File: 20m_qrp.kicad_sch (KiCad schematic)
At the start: 28 parts

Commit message: Export schematic for online viewing
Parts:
- gave numbers to parts that had none: 28
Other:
- company: (none) -> BARC <https://bellbrookarc.org/>
- title: (none) -> 20m QRP transceiver

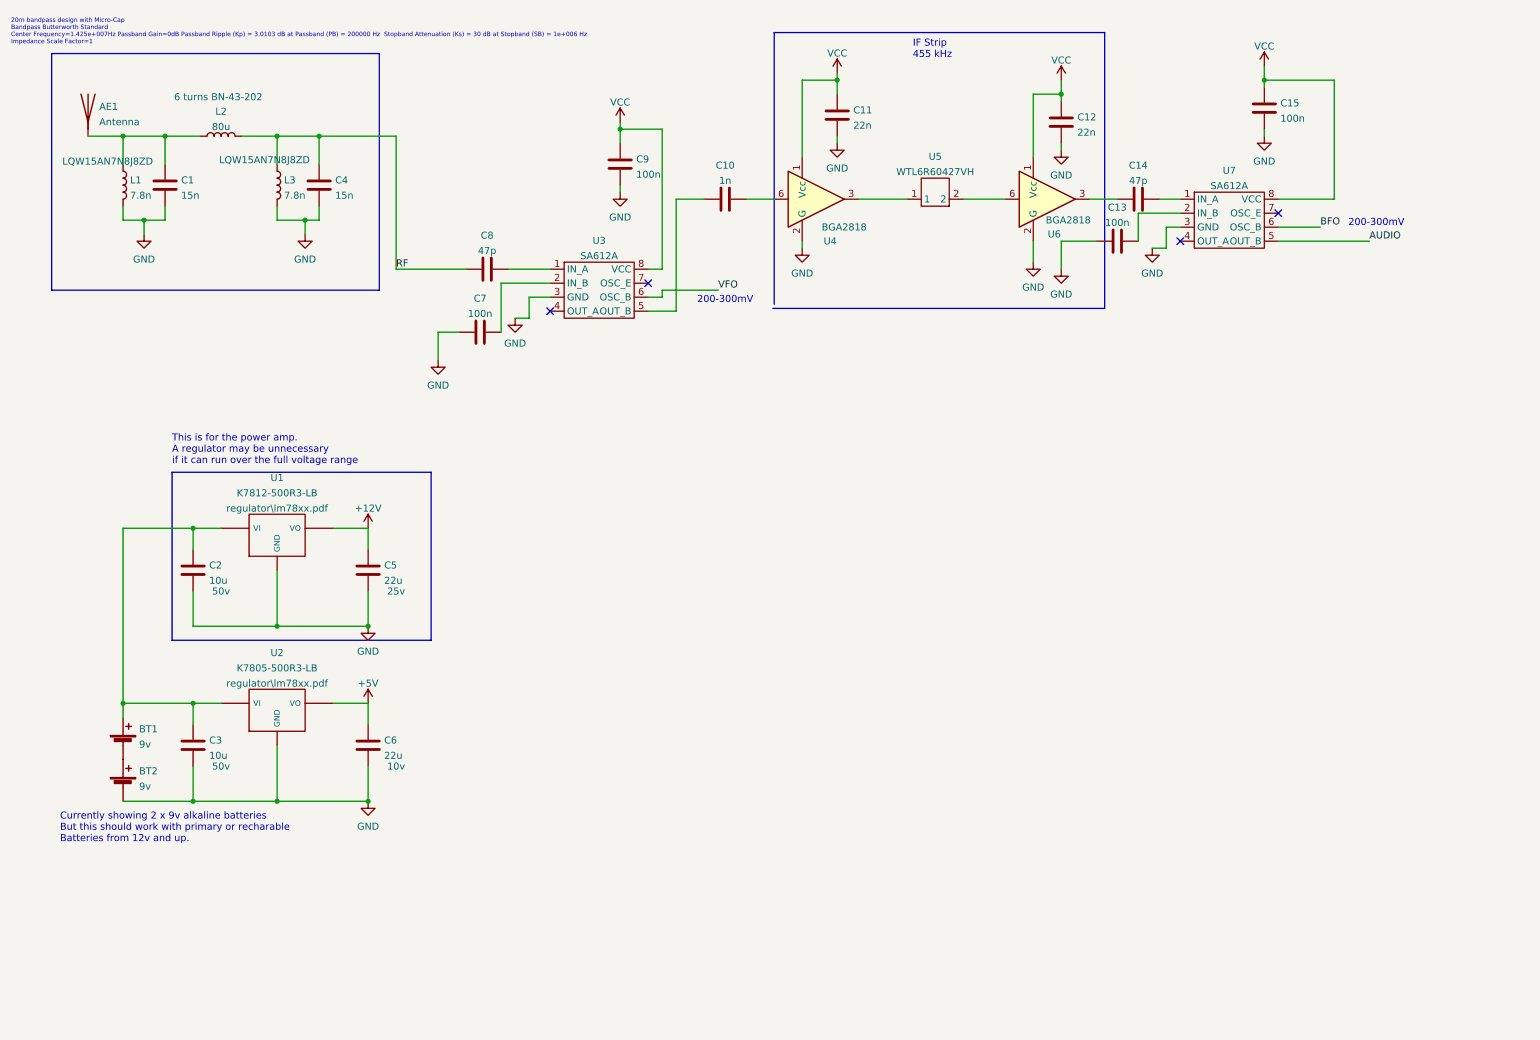
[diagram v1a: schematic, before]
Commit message: Add IF filter match and oscillator sections
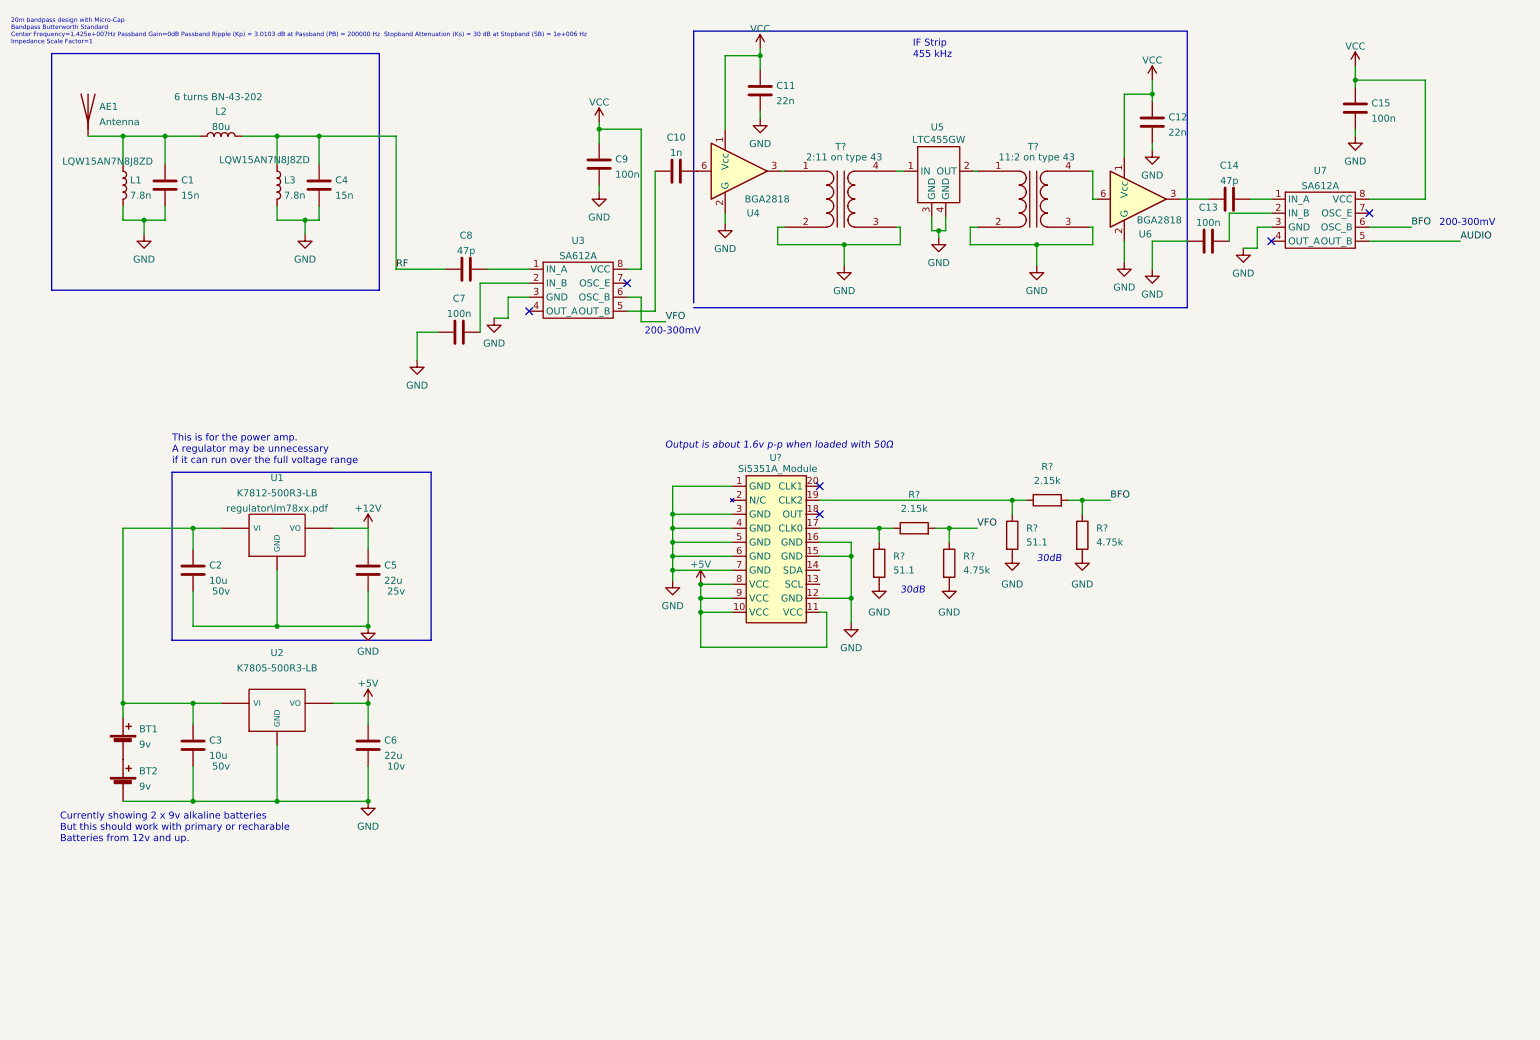
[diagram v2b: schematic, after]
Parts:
- added R? (x2): 51.1, symbol Device:R
- added R? (x2): 2.15k, symbol Device:R
- added R? (x2): 4.75k, symbol Device:R
- added T?: 2:11 on type 43, symbol Device:Transformer_1P_1S
- added T?: 11:2 on type 43, symbol Device:Transformer_1P_1S
- added U?: Si5351A_Module, symbol components:Si5351A_Module
- U5: value WTL6R60427VH -> LTC455GW
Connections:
- net +5V: now also U?.10 (VCC), U?.11 (VCC), U?.8 (VCC), U?.9 (VCC)
- net BFO: now also R?.1, R?.2
- net GND: now also U5.3 (GND), U5.4 (GND), R?.2, R?.2, R?.2, R?.2, T?.2 (AB), T?.2 (AB), T?.3 (SA), T?.3 (SA), U?.1 (GND), U?.12 (GND), U?.15 (GND), U?.16 (GND), U?.3 (GND), U?.4 (GND), U?.5 (GND), U?.6 (GND), U?.7 (GND)
- net VFO: now also R?.1, R?.2
- net at U4.3: now also T?.1 (AA); no longer U5.1
- net at U5.2 (OUT): now also T?.1 (AA); no longer U6.6
- new net: T?.4 (SB), U5.1 (IN)
- new net: R?.1, R?.1, U?.17 (CLK0)
- new net: R?.1, R?.1, U?.19 (CLK2)
- new net: T?.4 (SB), U6.6
- no-connect marks 4 -> 6
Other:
- note added: "30dB"
- note added: "Output is about 1.6v p-p when loaded with 50Ω"
- moved on the sheet: C10, C11, C12, C13, C14, C15, C7, C8, C9, U3, U4, U6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

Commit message: Add audio stage simulation
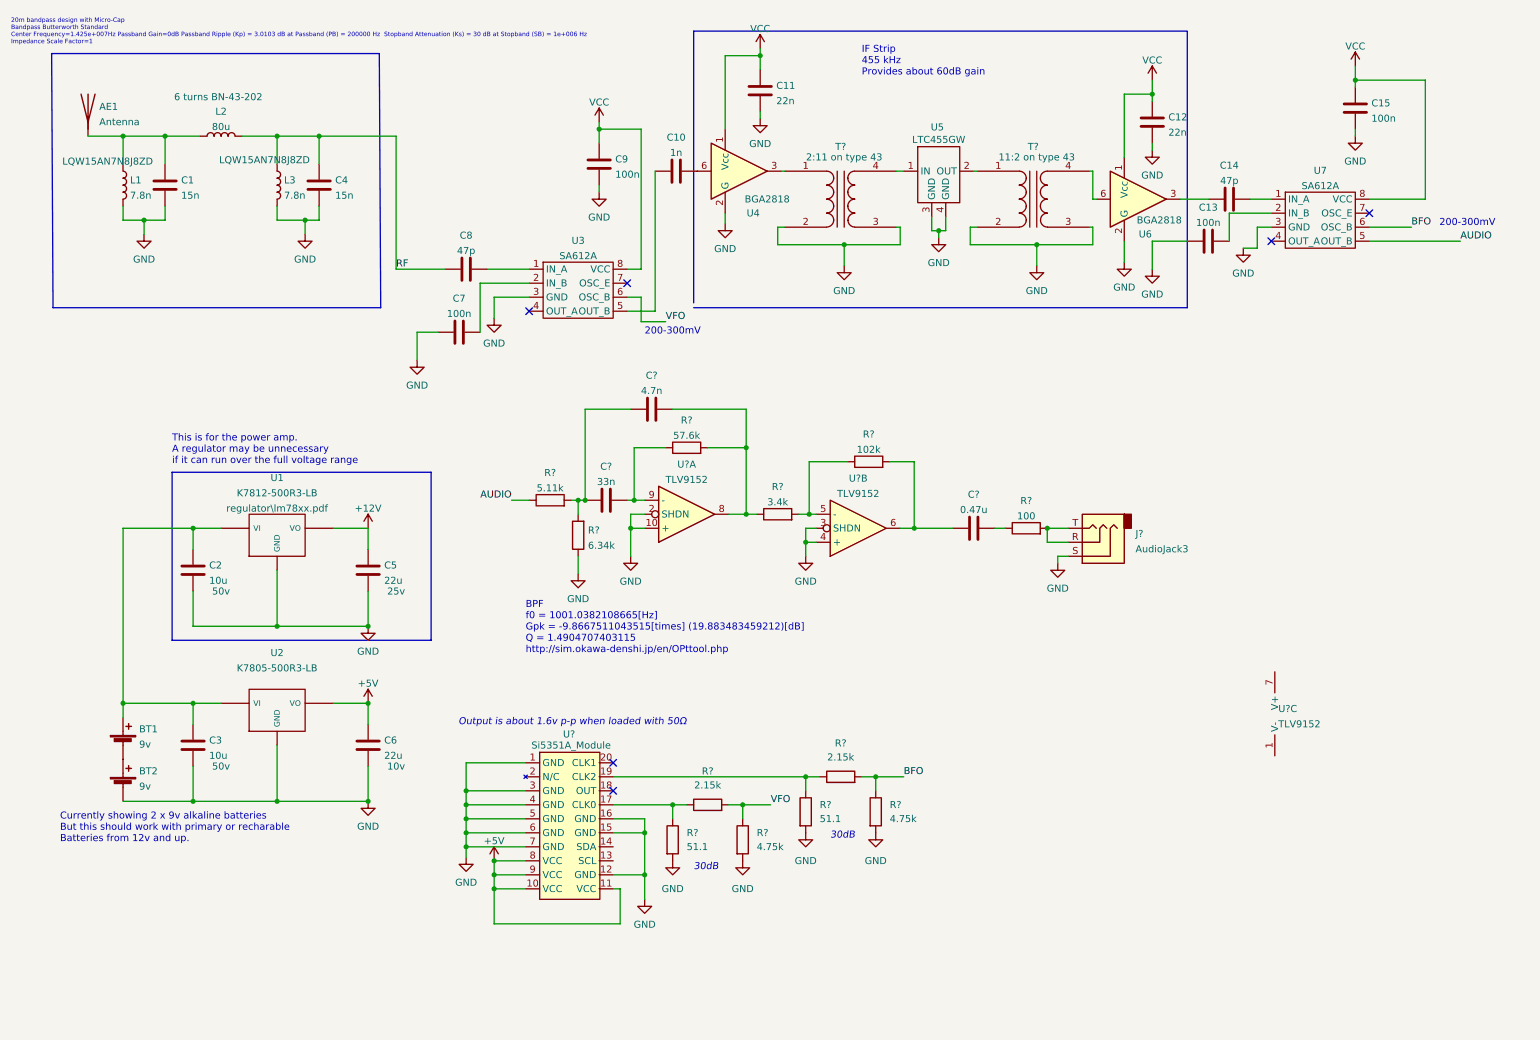
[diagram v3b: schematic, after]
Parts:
- added C?: 33n, symbol Device:C
- added C?: 4.7n, symbol Device:C
- added C?: 0.47u, symbol Device:C
- added J?: AudioJack3, symbol Connector:AudioJack3
- added R?: 102k, symbol Device:R
- added R?: 6.34k, symbol Device:R
- added R?: 3.4k, symbol Device:R
- added R?: 100, symbol Device:R
- added R?: 5.11k, symbol Device:R
- added R?: 57.6k, symbol Device:R
- added U? (x3): TLV9152, symbol components:TLV9152
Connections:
- net AUDIO: now also R?.1
- net GND: now also J?.S, R?.1, U?.10 (+), U?.2 (SHDN), U?.3 (SHDN), U?.4 (+)
- new net: C?.2, R?.1, R?.2, U?.8
- new net: C?.2, R?.1, U?.9 (-)
- new net: C?.1, C?.1, R?.2, R?.2
- new net: R?.1, R?.2, U?.5 (-)
- new net: C?.1, R?.2, U?.6
- new net: J?.R, J?.T, R?.2
- new net: C?.2, R?.1
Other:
- note added: "BPF f0 = 1001.0382108665[Hz] Gpk = -9.8667511043515[times] (19.883483459212)[dB] Q = 1.4904707403115 http://sim.okawa-denshi.jp/en/OPttool.php"
- note added: "IF Strip 455 kHz Provides about 60dB gain"
- note removed: "IF Strip 455 kHz"
- moved on the sheet: R?, U?

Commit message: Add mic stage
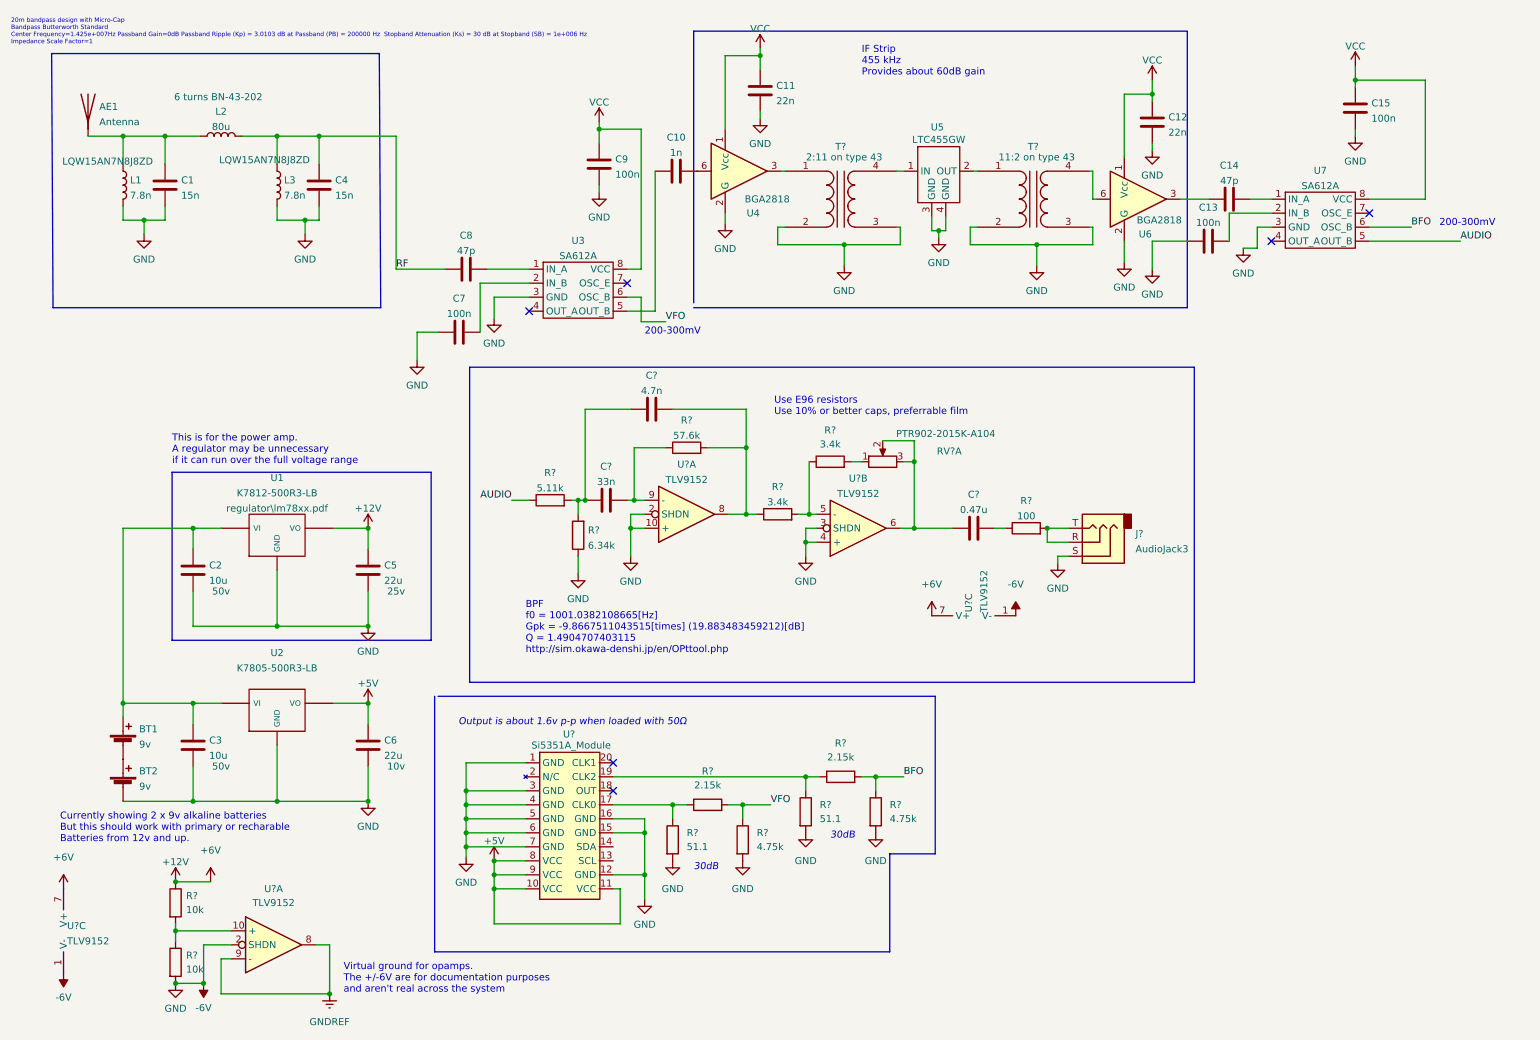
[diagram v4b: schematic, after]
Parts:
- added R? (x2): 10k, symbol Device:R
- added RV?: PTR902-2015K-A104, symbol Device:R_Potentiometer_Dual_Separate
- added U? (x2): TLV9152, symbol components:TLV9152
- R?: value 102k -> 3.4k
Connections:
- net GND is gone; now on net -6V: BT2.2 (-), C1.2, C11.2, C12.2, C13.1, C15.2, C2.2, C3.2, C4.2, C5.2, C6.2, C7.1, C9.2, J?.S, L1.2, L3.2, R?.1, R?.2, R?.2, R?.2, R?.2, T?.2 (AB), T?.2 (AB), T?.3 (SA), T?.3 (SA), U1.2 (GND), U2.2 (GND), U3.3 (GND), U4.2 (G), U4.4 (G), U4.5 (G), U5.3 (GND), U5.4 (GND), U6.2 (G), U6.4 (G), U6.5 (G), U7.3 (GND), U?.1 (GND), U?.10 (+), U?.12 (GND), U?.15 (GND), U?.16 (GND), U?.2 (SHDN), U?.3 (GND), U?.3 (SHDN), U?.4 (+), U?.4 (GND), U?.5 (GND), U?.6 (GND), U?.7 (GND)
- net +12V: now also U?.7 (V+), R?.1, U?.7 (V+)
- net at C?.1, U?.6: now also RV?.2, RV?.3; no longer R?.2
- net -6V: now reaches U?.1 (V-)
- net -6V: now also R?.2, U?.1 (V-), U?.2 (SHDN)
- new net: R?.2, RV?.1
- new net: R?.1, R?.2, U?.10 (+)
- new net GNDREF: U?.8, U?.9 (-)
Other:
- note added: "Use E96 resistors Use 10% or better caps, preferrable film"
- note added: "Virtual ground for opamps. The +/-6V are for documentation purposes and aren't real across the system"
- moved on the sheet: R?, U?C
